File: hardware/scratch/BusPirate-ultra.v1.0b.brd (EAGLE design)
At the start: 100 x 50 mm, 168 parts, among them IC1 23LC1024, IC10 SN74LVC1T45DBV, IC11 SN74LVC1T45DBV, IC12 74LVC1G07DBV, IC13 SN74LVC1T45DBV, IC17 74LVC1G07DBV, IC18 SN74LVC1T45DBV, IC19 74LVC1G07DBV, IC2 23LC1024, IC20 SN74LVC1T45DBV, IC21 74LVC1G07DBV, IC22 SN74LVC1T45DBV, IC23 MCP1824_ADJ, IC24 74HCT4051, IC4 74LVC1G07DBV, IC5 74LVC1G07DBV, IC6 74LVC1G07DBV, IC7 74LVC1G07DBV, IC8 SN74LVC1T45DBV, IC9 SN74LVC1T45DBV, J2 CON_HEADER_1X04, J4 CON_HEADER_1X10-RIGHT_ANGLED_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, Q1 DMMT3906W, U1 W25X40CL, U2 STM32F103ZX, U3 ICE40HX4K, U4 MCP6001, U5 74LVC245A, U7 MCP6001, U8 74HCT4066PW, U9 74HCT4066PW

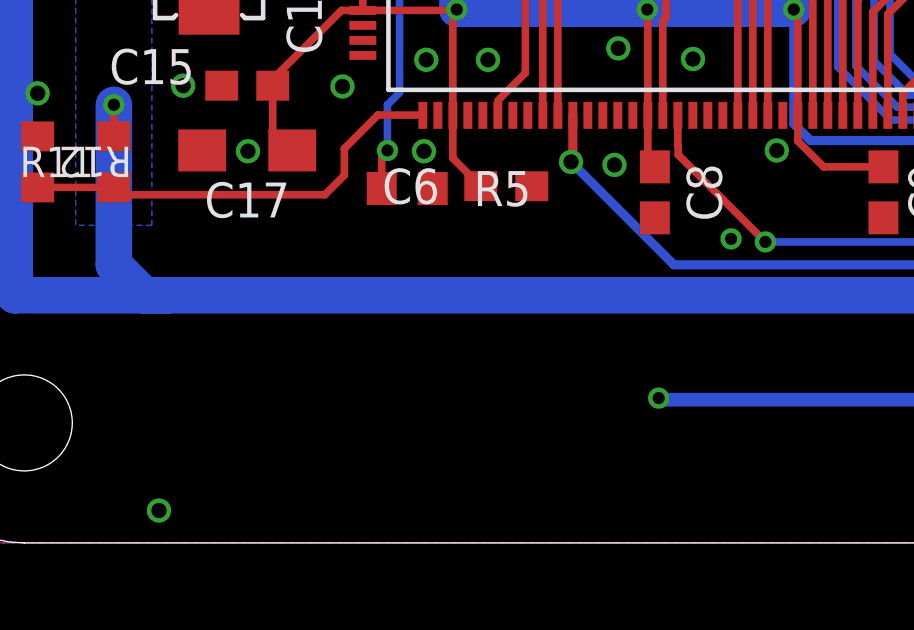
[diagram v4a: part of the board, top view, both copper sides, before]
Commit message: added 10pin header for display
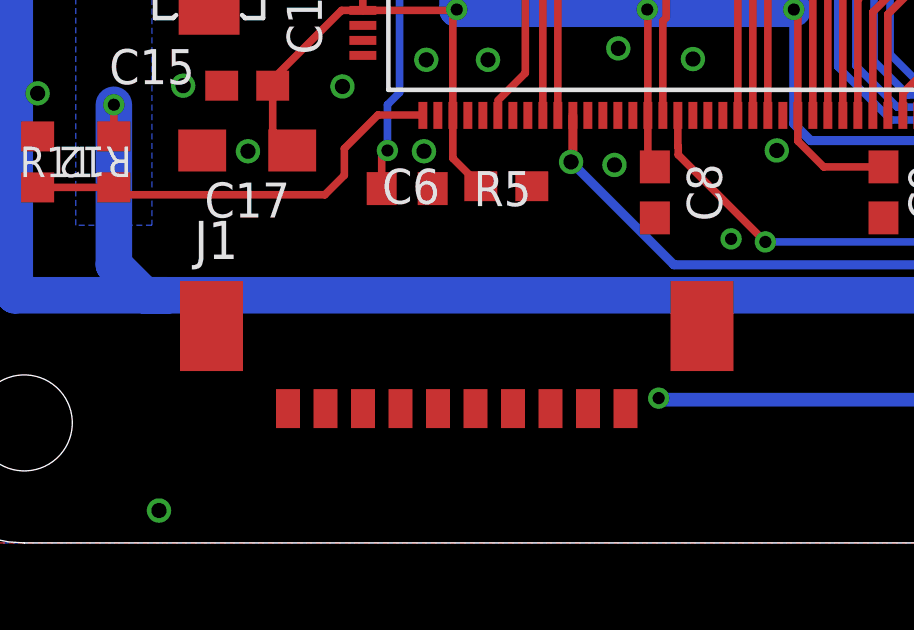
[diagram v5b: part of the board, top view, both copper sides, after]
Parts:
- added J1: CON_MOLEX_MALE_SMT_SH_1.25, dp_devices.v6:MOLEX_533980771
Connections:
- new net DISPLAY_CS: J1.P4
- new net DISPLAY_D/P: J1.P5
- new net N$62: J1.P8
- new net N$63: J1.P9
- new net N$66: J1.P10
- net 3V3: now also J1.P6
- net DISPLAY_SPI_CLOCK: now also J1.P1
- net DISPLAY_SPI_MISO: now also J1.P2
- net DISPLAY_SPI_MOSI: now also J1.P3
- net GND: now also J1.P7
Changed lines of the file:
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@@
 <layers>
 <layer number="1" name="Top" color="4" fill="1" visible="yes" active="yes"/>
-<layer number="16" name="Bottom" color="1" fill="1" visible="no" active="yes"/>
+<layer number="16" name="Bottom" color="1" fill="1" visible="yes" active="yes"/>
 <layer number="17" name="Pads" color="2" fill="1" visible="yes" active="yes"/>
 <layer number="18" name="Vias" color="2" fill="1" visible="yes" active="yes"/>
@@
 <layer number="20" name="Dimension" color="15" fill="1" visible="yes" active="yes"/>
 <layer number="21" name="tPlace" color="7" fill="1" visible="yes" active="yes"/>
-<layer number="22" name="bPlace" color="7" fill="1" visible="no" active="yes"/>
+<layer number="22" name="bPlace" color="7" fill="1" visible="yes" active="yes"/>
 <layer number="23" name="tOrigins" color="15" fill="1" visible="yes" active="yes"/>
-<layer number="24" name="bOrigins" color="15" fill="1" visible="no" active="yes"/>
-<layer number="25" name="tNames" color="7" fill="1" visible="no" active="yes"/>
-<layer number="26" name="bNames" color="7" fill="1" visible="no" active="yes"/>
+<layer number="24" name="bOrigins" color="15" fill="1" visible="yes" active="yes"/>
+<layer number="25" name="tNames" color="7" fill="1" visible="yes" active="yes"/>
+<layer number="26" name="bNames" color="7" fill="1" visible="yes" active="yes"/>
 <layer number="27" name="tValues" color="7" fill="1" visible="no" active="yes"/>
 <layer number="28" name="bValues" color="7" fill="1" visible="no" active="yes"/>
@@
 <layer number="38" name="bTest" color="7" fill="1" visible="no" active="yes"/>
 <layer number="39" name="tKeepout" color="4" fill="11" visible="yes" active="yes"/>
-<layer number="40" name="bKeepout" color="1" fill="11" visible="no" active="yes"/>
+<layer number="40" name="bKeepout" color="1" fill="11" visible="yes" active="yes"/>
 <layer number="41" name="tRestrict" color="4" fill="10" visible="yes" active="yes"/>
-<layer number="42" name="bRestrict" color="1" fill="10" visible="no" active="yes"/>
+<layer number="42" name="bRestrict" color="1" fill="10" visible="yes" active="yes"/>
 <layer number="43" name="vRestrict" color="2" fill="10" visible="no" active="yes"/>
 <layer number="44" name="Drills" color="7" fill="1" visible="no" active="yes"/>
@@
 <layer number="50" name="dxf" color="7" fill="1" visible="no" active="yes"/>
 <layer number="51" name="tDocu" color="7" fill="1" visible="yes" active="yes"/>
-<layer number="52" name="bDocu" color="7" fill="1" visible="no" active="yes"/>
+<layer number="52" name="bDocu" color="7" fill="1" visible="yes" active="yes"/>
 <layer number="53" name="tGND_GNDA" color="7" fill="9" visible="no" active="no"/>
 <layer number="54" name="bGND_GNDA" color="1" fill="9" visible="no" active="no"/>
@@
 <element name="U9" library="dp_devices.v6" package="TSSOP-14" value="74HCT4066PW" x="88.9" y="6.35"/>
 <element name="U5" library="dp_devices.v6" package="TSSOP-20" value="74LVC245A" x="76.835" y="23.495" rot="R270"/>
+<element name="J1" library="dp_devices.v6" package="MOLEX_533980771" value="CON_MOLEX_MALE_SMT_SH_1.25" x="18.415" y="5.715"/>
 </elements>
 <signals>
@@
 <contactref element="U5" pad="19"/>
 <contactref element="U5" pad="10"/>
+<contactref element="J1" pad="P7"/>
 <wire x1="90.85" y1="41.115" x2="99.1121" y2="41.1833" width="0" layer="19" extent="1-1"/>
 <wire x1="84.201" y1="41.006" x2="90.85" y2="41.115" width="0" layer="19" extent="1-1"/>
@@
 <wire x1="8.48995" y1="1.079875" x2="1.2446" y2="8.8237" width="0" layer="19" extent="1-1"/>
 <wire x1="99.1121" y1="25.0035" x2="89.789" y2="18.669" width="0" layer="19" extent="1-1"/>
+<wire x1="16.54" y1="4.477" x2="8.48995" y2="1.079875" width="0" layer="19" extent="1-1"/>
 </signal>
 <signal name="3V3">
@@
 <wire x1="78.32" y1="27.94" x2="79.535" y2="27.94" width="0.254" layer="1"/>
 <wire x1="79.535" y1="27.94" x2="79.535" y2="26.42" width="0.254" layer="1"/>
+<contactref element="J1" pad="P6"/>
 <wire x1="80.0106875" y1="43.7146875" x2="82.299" y2="40.909" width="0" layer="19" extent="1-1"/>
 <wire x1="78.598" y1="44.958" x2="79.499" y2="43.703" width="0" layer="19" extent="1-1"/>
@@
 <wire x1="17.614" y1="11.811" x2="18.285" y2="12.821" width="0" layer="19" extent="1-1"/>
 <wire x1="69.2" y1="18.415" x2="67.945" y2="18.542" width="0" layer="19" extent="1-16"/>
+<wire x1="43.18" y1="41.275" x2="41.91" y2="41.275" width="0" layer="19" extent="16-16"/>
 <wire x1="55.841" y1="44.45" x2="57.15" y2="44.45" width="0" layer="19" extent="1-1"/>
 <wire x1="77.597" y1="15.001" x2="76.2" y2="14.3002" width="0" layer="19" extent="1-16"/>
@@
 <wire x1="82.299" y1="14.366" x2="81.28" y2="16.891" width="0" layer="19" extent="1-16"/>
 <wire x1="68.834" y1="31.765" x2="70.736" y2="33.924" width="0" layer="19" extent="1-1"/>
+<wire x1="39.79" y1="36.37" x2="36.785" y2="35.351" width="0" layer="19" extent="1-1"/>
+<wire x1="39.685" y1="38.88" x2="39.79" y2="36.37" width="0" layer="19" extent="1-1"/>
 <wire x1="77.597" y1="31.765" x2="73.536" y2="31.13" width="0" layer="19" extent="1-1"/>
 <wire x1="79.499" y1="33.924" x2="77.597" y2="31.765" width="0" layer="19" extent="1-1"/>
@@
 <wire x1="70.373" y1="9.271" x2="70.736" y2="8.016" width="0" layer="19" extent="1-1"/>
 <wire x1="68.707" y1="5.842" x2="70.736" y2="8.016" width="0" layer="19" extent="1-1"/>
+<wire x1="17.79" y1="4.477" x2="12.93" y2="13.081" width="0" layer="19" extent="1-1"/>
 </signal>
 <signal name="N$7">
@@
 <wire x1="60.706" y1="13.589" x2="60.706" y2="12.94496875" width="0.254" layer="16"/>
 <wire x1="59.9186" y1="31.623" x2="59.9186" y2="32.893" width="0.254" layer="1"/>
-<wire x1="6.32" y1="39.055" x2="25.7984" y2="12.9366" width="0" layer="19" extent="1-1"/>
+<wire x1="25.785" y1="14.25" x2="6.32" y2="39.055" width="0" layer="19" extent="1-1"/>
 </signal>
 <signal name="N$18">
@@
 <contactref element="U9" pad="14"/>
 <contactref element="C65" pad="1"/>
+<wire x1="3.683" y1="8.255" x2="8.763" y2="8.255" width="1.2192" layer="16"/>
 <wire x1="85.305" y1="46.99" x2="86.95" y2="46.715" width="0" layer="19" extent="1-1"/>
 <wire x1="86.95" y1="9.25" x2="86.95" y2="46.715" width="0" layer="19" extent="1-1"/>
@@
 <wire x1="52.009" y1="5.745" x2="58.895" y2="3.44" width="0" layer="19" extent="1-1"/>
 <wire x1="41.275" y1="8.255" x2="50.38" y2="8.636" width="0" layer="19" extent="1-16"/>
-<wire x1="3.683" y1="8.255" x2="8.763" y2="8.255" width="1.2192" layer="16"/>
+<wire x1="4.66" y1="43.561" x2="4.699" y2="42.037" width="0" layer="19" extent="1-1"/>
 </signal>
 <signal name="EXVUSB">
@@
 <contactref element="U2" pad="40"/>
 <contactref element="R48" pad="1"/>
-<wire x1="2.325" y1="46.355" x2="18.785" y2="14.25" width="0" layer="19" extent="1-1"/>
+<wire x1="18.785" y1="14.25" x2="2.325" y2="46.355" width="0" layer="19" extent="1-1"/>
 </signal>
 <signal name="N$15">
@@
 <signal name="DISPLAY_SPI_CLOCK">
 <contactref element="U2" pad="41"/>
+<contactref element="J1" pad="P1"/>
+<wire x1="24.04" y1="4.477" x2="19.285" y2="14.25" width="0" layer="19" extent="1-1"/>
 </signal>
 <signal name="DISPLAY_SPI_MOSI">
 <contactref element="U2" pad="43"/>
+<contactref element="J1" pad="P3"/>
+<wire x1="21.54" y1="4.477" x2="20.285" y2="14.25" width="0" layer="19" extent="1-1"/>
 </signal>
 <signal name="DISPLAY_SPI_MISO">
 <contactref element="U2" pad="42"/>
+<contactref element="J1" pad="P2"/>
+<wire x1="22.79" y1="4.477" x2="19.785" y2="14.25" width="0" layer="19" extent="1-1"/>
 </signal>
 <signal name="N$3">
@@
 <wire x1="88.9" y1="5.08" x2="88.9" y2="3.65" width="0.254" layer="1"/>
 </signal>
+<signal name="DISPLAY_CS">
+<contactref element="J1" pad="P4"/>
+</signal>
+<signal name="DISPLAY_D/P">
+<contactref element="J1" pad="P5"/>
+</signal>
+<signal name="N$62">
+<contactref element="J1" pad="P8"/>
+</signal>
+<signal name="N$63">
+<contactref element="J1" pad="P9"/>
+</signal>
+<signal name="N$66">
+<contactref element="J1" pad="P10"/>
+</signal>
 </signals>
